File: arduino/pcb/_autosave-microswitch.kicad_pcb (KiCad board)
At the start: 2 copper layers, 10 parts, among them P1 CONN_01X08, P2 CONN_01X02, P3 CONN_01X02, P4 CONN_01X02, P5 CONN_01X02, P6 CONN_01X08

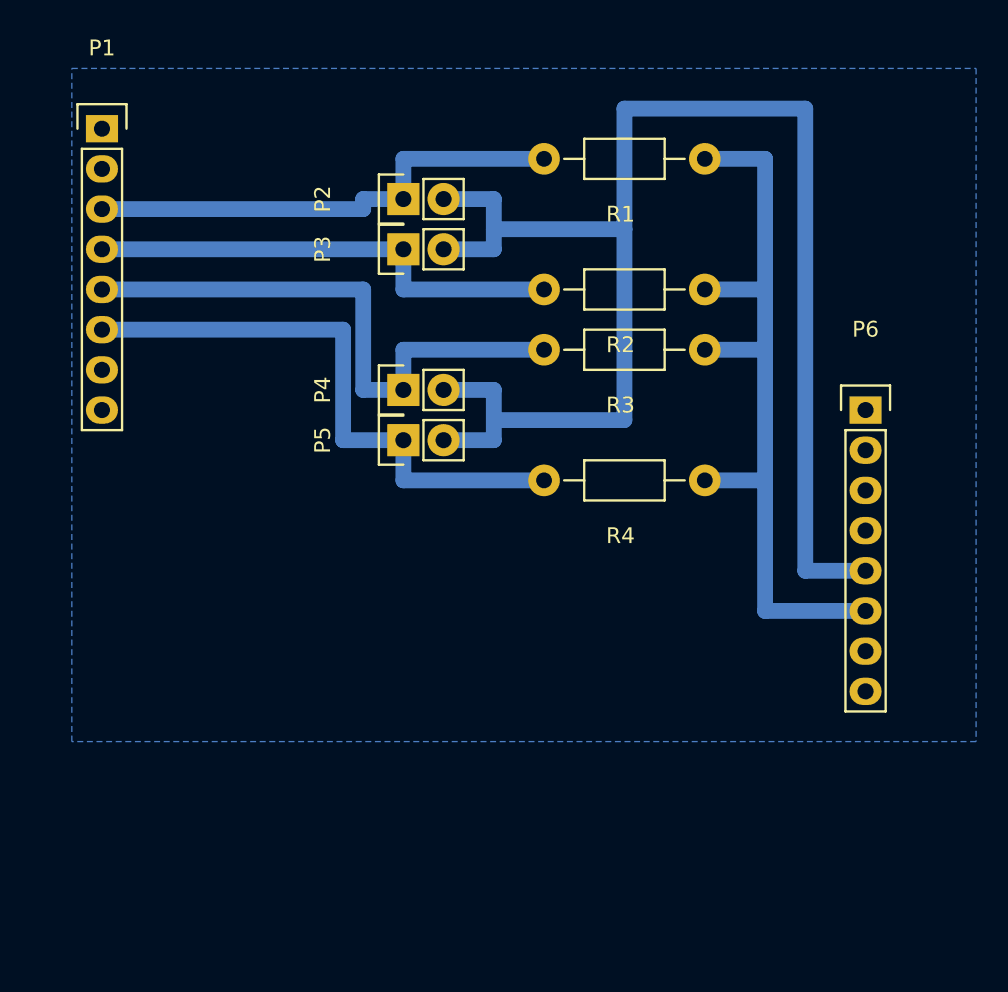
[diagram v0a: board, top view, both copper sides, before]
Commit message: Rework enemy animations code. Add dialogs in cutscenes. Finish first custscene and stage
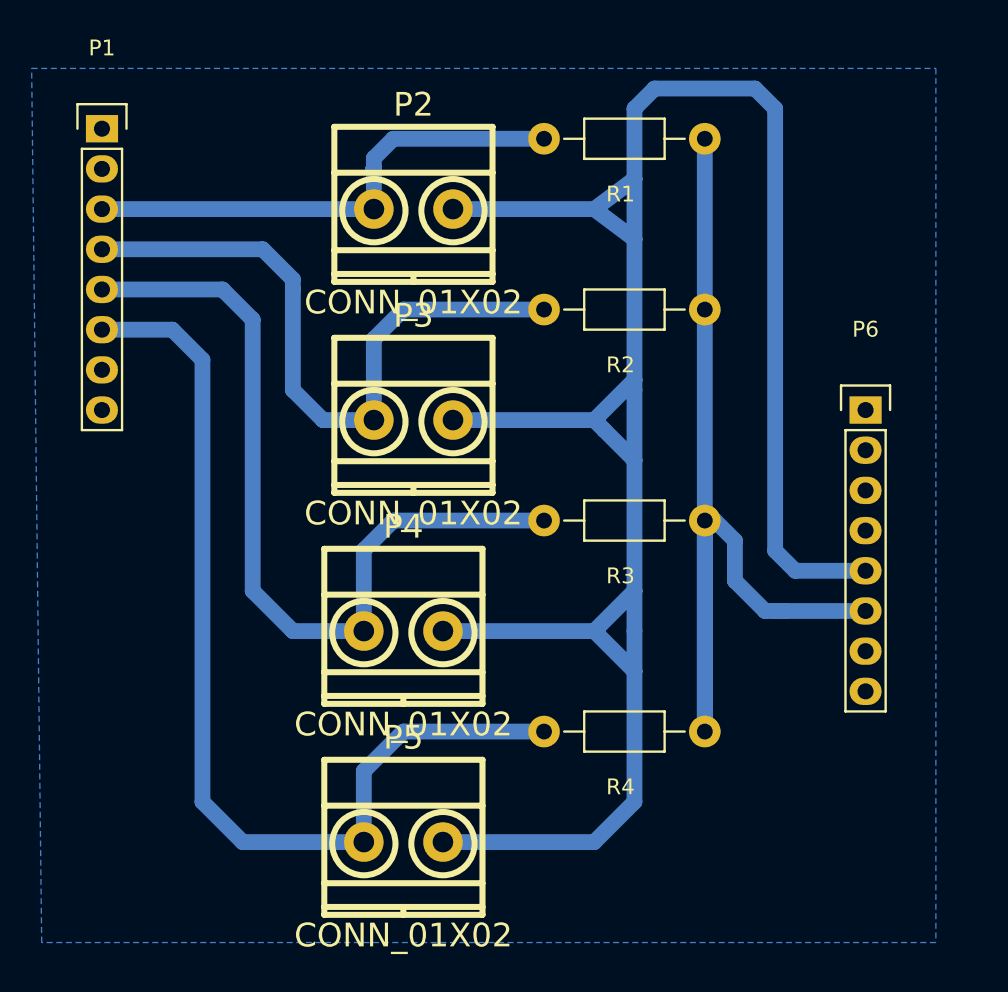
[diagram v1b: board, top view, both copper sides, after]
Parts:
- P2, P3, P4, P5: footprint Pin_Headers:Pin_Header_Straight_1x02 -> bornera:mkds_1,5-2
- moved P5 25.4 mm to (134.6, 146.7), turned to 0 degrees
- moved R4 15.9 mm to (153.7, 139.7)
- moved P4 15.2 mm to (134.6, 133.3), turned to 0 degrees
- moved P3 10.8 mm to (135.3, 120.0), turned to 0 degrees
- moved R3 10.8 mm to (153.7, 126.4)
- moved R1 1.27 mm to (153.7, 102.2)
- moved R2 1.27 mm to (153.7, 113.0)
- moved P2 0.90 mm to (135.3, 106.7), turned to 0 degrees
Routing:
- net +5V: track 99.7 -> 149.9 mm
- net Net-(P1-Pad6): track 37.5 -> 63.3 mm
- net Net-(P1-Pad5): track 36.8 -> 52.8 mm
- net GND: track 50.2 -> 64.8 mm
- net Net-(P1-Pad4): track 30.5 -> 42.4 mm
- net Net-(P1-Pad3): track 31.1 -> 31.7 mm
